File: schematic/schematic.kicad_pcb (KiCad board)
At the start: 2 copper layers, 99.1 x 99.1 mm, 0 parts

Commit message: d
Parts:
- added AE1: Antenna_Chip, RF_Antenna:Johanson_2450AT18x100, F.Cu at (220.8, 44.4)
- added BT1: Battery_Cell, Connector_PinHeader_2.54mm:PinHeader_1x02_P2.54mm_Vertical, F.Cu at (99.9, 69.8)
- added BT2: Battery_Cell, Connector_PinHeader_2.54mm:PinHeader_1x02_P2.54mm_Vertical, F.Cu at (100.1, 77.1)
- added BT3: Battery_Cell, Connector_PinHeader_2.54mm:PinHeader_1x02_P2.54mm_Vertical, F.Cu at (100.3, 84.6)
- added C1: 3.797pF, Capacitor_SMD:C_0805_2012Metric_Pad1.18x1.45mm_HandSolder, F.Cu at (230.8, 44.2)
- added C10: 100nF, Capacitor_SMD:C_0805_2012Metric_Pad1.18x1.45mm_HandSolder, F.Cu at (226.0, 44.2)
- added C11: 84nF, Capacitor_SMD:C_0805_2012Metric_Pad1.18x1.45mm_HandSolder, F.Cu at (198.0, 44.2)
- added C12: 1uF, Capacitor_SMD:C_0805_2012Metric_Pad1.18x1.45mm_HandSolder, F.Cu at (193.2, 50.2)
- added C13: 1uF, Capacitor_SMD:C_0805_2012Metric_Pad1.18x1.45mm_HandSolder, F.Cu at (193.2, 47.2)
- added C14: 100nF, Capacitor_SMD:C_0805_2012Metric_Pad1.18x1.45mm_HandSolder, F.Cu at (185.5, 44.0)
- added C15: 10uF, Capacitor_SMD:C_0805_2012Metric_Pad1.18x1.45mm_HandSolder, F.Cu at (111.4, 60.9)
- added C16: 100nF, Capacitor_SMD:C_0805_2012Metric_Pad1.18x1.45mm_HandSolder, F.Cu at (176.7, 61.3)
- added C19: 10uF, Capacitor_SMD:C_0805_2012Metric_Pad1.18x1.45mm_HandSolder, F.Cu at (176.7, 64.3)
- added C2: 4.64pF, Capacitor_SMD:C_0805_2012Metric_Pad1.18x1.45mm_HandSolder, F.Cu at (229.9, 47.2)
- added C20: 10uF, Capacitor_SMD:C_0805_2012Metric_Pad1.18x1.45mm_HandSolder, F.Cu at (186.9, 56.8)
- added C21: 100nF, Capacitor_SMD:C_0805_2012Metric_Pad1.18x1.45mm_HandSolder, F.Cu at (107.9, 61.0)
- added C22: 1uF, Capacitor_SMD:C_0805_2012Metric_Pad1.18x1.45mm_HandSolder, F.Cu at (181.1, 58.2)
- added C23: 1uF, Capacitor_SMD:C_0805_2012Metric_Pad1.18x1.45mm_HandSolder, F.Cu at (155.8, 80.0)
- added C3: 3.3nF, Capacitor_SMD:C_0805_2012Metric_Pad1.18x1.45mm_HandSolder, F.Cu at (219.7, 54.4)
- added C4: 10nF, Capacitor_SMD:C_0805_2012Metric_Pad1.18x1.45mm_HandSolder, F.Cu at (224.5, 50.6)
- added C5: 100nF, Capacitor_SMD:C_0805_2012Metric_Pad1.18x1.45mm_HandSolder, F.Cu at (225.1, 47.6)
- added C6: 10pF, Capacitor_SMD:C_0805_2012Metric_Pad1.18x1.45mm_HandSolder, F.Cu at (220.3, 47.6)
- added C7: 10pF, Capacitor_SMD:C_0805_2012Metric_Pad1.18x1.45mm_HandSolder, F.Cu at (219.7, 51.4)
- added C8: 100nF, Capacitor_SMD:C_0805_2012Metric_Pad1.18x1.45mm_HandSolder, F.Cu at (224.5, 53.6)
- added C9: 84nF, Capacitor_SMD:C_0805_2012Metric_Pad1.18x1.45mm_HandSolder, F.Cu at (174.4, 67.5)
- added D1: ZMM3V9, Diode_SMD:D_MiniMELF, F.Cu at (144.9, 96.4)
- added D2: ZMM3V9, Diode_SMD:D_MiniMELF, F.Cu at (138.6, 96.4)
- added D4: SS34, Diode_SMD:D_SMA_Handsoldering, B.Cu at (114.5, 62.3)
- added J1: Peltier Connection, Connector_PinHeader_2.54mm:PinHeader_1x02_P2.54mm_Vertical, F.Cu at (151.5, 88.7)
- added J2: USB_C_Receptacle_USB2.0, 1KicadLib:USB4125-GF-A, F.Cu at (103.4, 58.9)
- added J4: Serial, Connector_PinHeader_2.54mm:PinHeader_1x03_P2.54mm_Vertical, F.Cu at (139.9, 104.0)
- added L1: 1.807nH, Inductor_SMD:L_0805_2012Metric_Pad1.15x1.40mm_HandSolder, F.Cu at (235.6, 44.2)
- added L2: 33uH, Inductor_SMD:L_10.4x10.4_H4.8, F.Cu at (159.4, 48.7)
- added L3: 33uH, Inductor_SMD:L_10.4x10.4_H4.8, B.Cu at (119.1, 54.5)
- added L4: 33uH, Inductor_SMD:L_10.4x10.4_H4.8, F.Cu at (152.8, 66.1)
- added R1: 20k, Resistor_SMD:R_0805_2012Metric_Pad1.20x1.40mm_HandSolder, F.Cu at (229.3, 50.6)
- added R10: 7.5k, Resistor_SMD:R_0805_2012Metric_Pad1.20x1.40mm_HandSolder, F.Cu at (181.5, 61.2)
- added R11: 15k, Resistor_SMD:R_0805_2012Metric_Pad1.20x1.40mm_HandSolder, F.Cu at (137.1, 116.9)
- added R12: 28.7, Resistor_SMD:R_2512_6332Metric_Pad1.40x3.35mm_HandSolder, F.Cu at (106.0, 71.3)
- added R13: 33k, Resistor_SMD:R_0805_2012Metric_Pad1.20x1.40mm_HandSolder, F.Cu at (191.7, 56.8)
- added R14: 110k, Resistor_SMD:R_0805_2012Metric_Pad1.20x1.40mm_HandSolder, F.Cu at (136.5, 120.8)
- added R15: 28.7, Resistor_SMD:R_2512_6332Metric_Pad1.40x3.35mm_HandSolder, F.Cu at (106.0, 79.4)
- added R16: 28.7, Resistor_SMD:R_2512_6332Metric_Pad1.40x3.35mm_HandSolder, F.Cu at (106.1, 87.5)
- added R17: 200, Resistor_SMD:R_0805_2012Metric_Pad1.20x1.40mm_HandSolder, F.Cu at (121.4, 70.2)
- added R18: 200, Resistor_SMD:R_0805_2012Metric_Pad1.20x1.40mm_HandSolder, F.Cu at (121.1, 77.9)
- added R19: 200, Resistor_SMD:R_0805_2012Metric_Pad1.20x1.40mm_HandSolder, F.Cu at (121.3, 86.1)
- added R2: 39k, Resistor_SMD:R_0805_2012Metric_Pad1.20x1.40mm_HandSolder, F.Cu at (165.4, 78.4)
- added R20: 90k, Resistor_SMD:R_0805_2012Metric_Pad1.20x1.40mm_HandSolder, F.Cu at (213.0, 65.6)
- added R21: 90k, Resistor_SMD:R_0805_2012Metric_Pad1.20x1.40mm_HandSolder, F.Cu at (213.0, 68.5)
- added R22: 180k, Resistor_SMD:R_0805_2012Metric_Pad1.20x1.40mm_HandSolder, F.Cu at (122.7, 102.6)
- added R23: 36k, Resistor_SMD:R_0805_2012Metric_Pad1.20x1.40mm_HandSolder, F.Cu at (119.4, 103.8)
- added R24: 90k, Resistor_SMD:R_0805_2012Metric_Pad1.20x1.40mm_HandSolder, F.Cu at (222.5, 62.6)
- added R25: 4.3k, Resistor_SMD:R_0805_2012Metric_Pad1.20x1.40mm_HandSolder, F.Cu at (123.0, 105.8)
- added R26: 180k, Resistor_SMD:R_0805_2012Metric_Pad1.20x1.40mm_HandSolder, F.Cu at (124.4, 99.6)
- added R27: 68k, Resistor_SMD:R_0805_2012Metric_Pad1.20x1.40mm_HandSolder, F.Cu at (123.4, 95.0)
- added R28: 510k, Resistor_SMD:R_0805_2012Metric_Pad1.20x1.40mm_HandSolder, F.Cu at (117.9, 95.6)
- added R29: 620k, Resistor_SMD:R_0805_2012Metric_Pad1.20x1.40mm_HandSolder, F.Cu at (118.4, 98.7)
- added R3: 39k, Resistor_SMD:R_0805_2012Metric_Pad1.20x1.40mm_HandSolder, F.Cu at (202.8, 44.2)
- added R30: 200k, Resistor_SMD:R_0805_2012Metric_Pad1.20x1.40mm_HandSolder, B.Cu at (105.2, 100.9)
- added R31: 51k, Resistor_SMD:R_0805_2012Metric_Pad1.20x1.40mm_HandSolder, B.Cu at (109.1, 100.9)
- added R33: 500, Resistor_SMD:R_0805_2012Metric_Pad1.20x1.40mm_HandSolder, F.Cu at (102.8, 97.7)
- added R34: 12.5k, Resistor_SMD:R_0805_2012Metric_Pad1.20x1.40mm_HandSolder, B.Cu at (106.5, 94.7)
- added R39: 150k, Resistor_SMD:R_0805_2012Metric_Pad1.20x1.40mm_HandSolder, F.Cu at (224.5, 56.6)
- added R4: .1, Resistor_SMD:R_1206_3216Metric_Pad1.30x1.75mm_HandSolder, F.Cu at (100.7, 91.9)
- added R40: 100k, Resistor_SMD:R_0805_2012Metric_Pad1.20x1.40mm_HandSolder, F.Cu at (234.7, 47.2)
- added R5: 1k, Resistor_SMD:R_0805_2012Metric_Pad1.20x1.40mm_HandSolder, F.Cu at (104.2, 93.6)
- added R6: 1k, Resistor_SMD:R_0805_2012Metric_Pad1.20x1.40mm_HandSolder, B.Cu at (107.5, 97.7)
- added R7: 12.5k, Resistor_SMD:R_0805_2012Metric_Pad1.20x1.40mm_HandSolder, B.Cu at (103.3, 94.6)
- added R8: 5.1k, Resistor_SMD:R_0805_2012Metric_Pad1.20x1.40mm_HandSolder, B.Cu at (104.3, 59.5)
- added R9: 5.1k, Resistor_SMD:R_0805_2012Metric_Pad1.20x1.40mm_HandSolder, B.Cu at (102.2, 57.4)
- added SW1: Power Switch, Connector_PinHeader_2.54mm:PinHeader_1x02_P2.54mm_Vertical, F.Cu at (114.1, 66.1)
- added TH1: SDNT2012X103F3950FTF, Resistor_SMD:R_0805_2012Metric_Pad1.20x1.40mm_HandSolder, F.Cu at (213.0, 62.6)
- added TH2: SDNT2012X103F3950FTF, Resistor_SMD:R_0805_2012Metric_Pad1.20x1.40mm_HandSolder, F.Cu at (217.8, 62.6)
- added TH3: SDNT2012X103F3950FTF, Resistor_SMD:R_0805_2012Metric_Pad1.20x1.40mm_HandSolder, F.Cu at (217.8, 65.6)
- added U1: ESP32-D-WD-V3, Package_DFN_QFN:QFN-48-1EP_5x5mm_P0.35mm_EP3.7x3.7mm, F.Cu at (222.0, 97.6)
- added U10: BSD316, Package_TO_SOT_SMD:SOT-363_SC-70-6_Handsoldering, B.Cu at (105.9, 82.9)
- added U11: BSD316, Package_TO_SOT_SMD:SOT-363_SC-70-6_Handsoldering, B.Cu at (105.9, 90.3)
- added U12: PC817, Package_DIP:DIP-4_W7.62mm, B.Cu at (118.3, 70.2)
- added U13: PC817, Package_DIP:DIP-4_W7.62mm, B.Cu at (118.1, 77.9)
- added U14: PC817, Package_DIP:DIP-4_W7.62mm, B.Cu at (118.2, 86.1)
- added U15: AS431, Package_TO_SOT_SMD:SOT-23-5_HandSoldering, F.Cu at (99.3, 97.7)
- added U17: XL6009, Package_TO_SOT_SMD:TO-263-5_TabPin3, F.Cu at (118.3, 53.0)
- added U18: slg55021, 1KicadLib:TDFN_8_2x2mm_EP_0.9x1.65mm, F.Cu at (150.9, 105.4)
- added U19: AOZ6662DI, 1KicadLib:DFN_8_3x3mm_EP_1.25x2.7mm, F.Cu at (184.1, 48.8)
- added U2: NL17SZ14, Package_TO_SOT_SMD:SOT-553, F.Cu at (155.5, 91.2)
- added U20: AOZ6662DI, 1KicadLib:DFN_8_3x3mm_EP_1.25x2.7mm, F.Cu at (169.4, 69.1)
- added U3: BUK9K52-60E, 1KicadLib:LFPAK56D, F.Cu at (148.4, 92.1)
- added U4: BUK9K52-60E, 1KicadLib:LFPAK56D, F.Cu at (141.5, 92.1)
- added U5: LM324, Package_SO:SOIC-14_3.9x8.7mm_P1.27mm, F.Cu at (109.1, 97.2)
- added U6: slg55021, 1KicadLib:TDFN_8_2x2mm_EP_0.9x1.65mm, F.Cu at (150.9, 101.1)
- added U7: NL17SZ14, Package_TO_SOT_SMD:SOT-553, F.Cu at (155.5, 88.0)
- added U8: NL17SZ14, Package_TO_SOT_SMD:SOT-553, F.Cu at (150.9, 95.2)
- added U9: BSD316, Package_TO_SOT_SMD:SOT-363_SC-70-6_Handsoldering, B.Cu at (105.9, 74.7)
- added Y1: Crystal_GND24, Crystal:Crystal_SMD_SeikoEpson_FA238-4Pin_3.2x2.5mm_HandSoldering, F.Cu at (214.0, 52.8)
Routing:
- net Net-(R30-Pad2): track 0.00 -> 1.27 mm, vias 0 -> 1
- net Net-(R5-Pad1): vias 0 -> 1
- net Net-(R34-Pad2): vias 0 -> 1
- net Net-(R34-Pad1): vias 0 -> 1

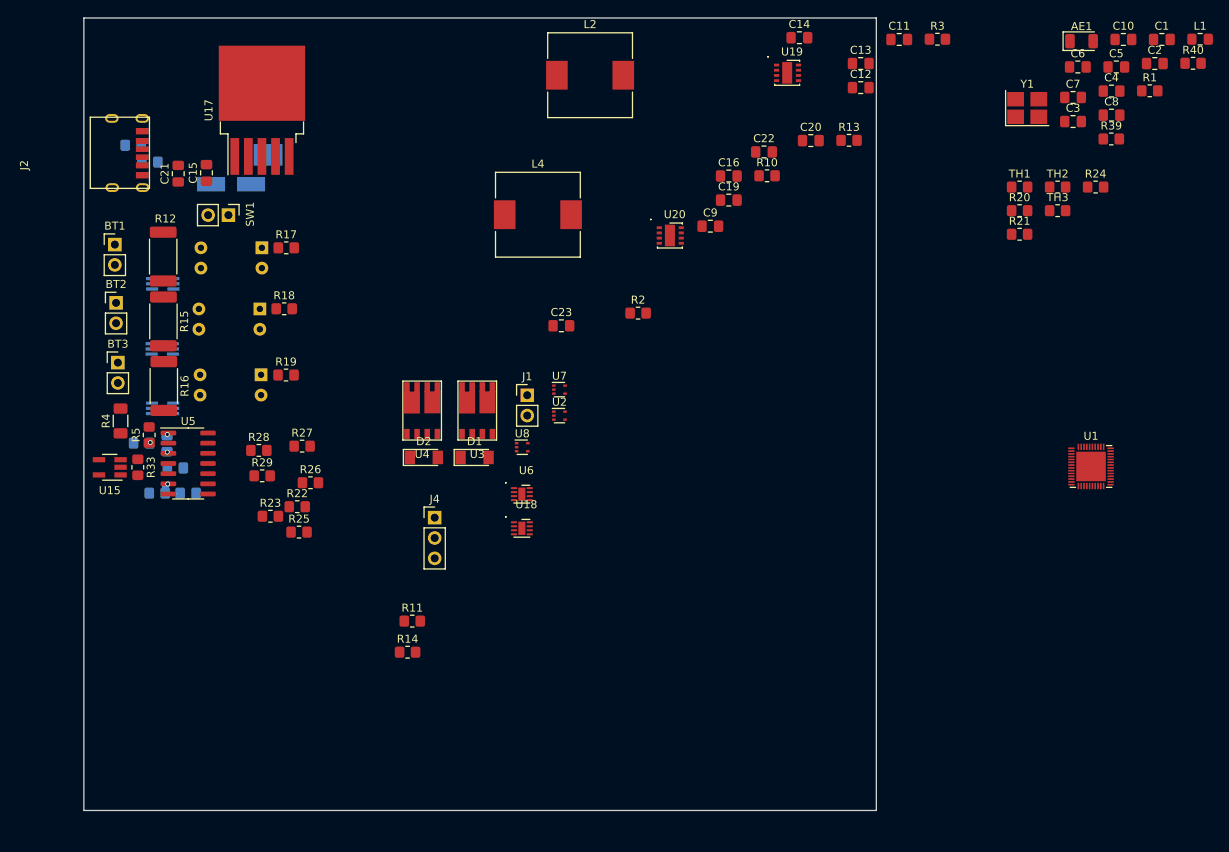
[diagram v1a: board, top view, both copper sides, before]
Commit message: beta boards routed
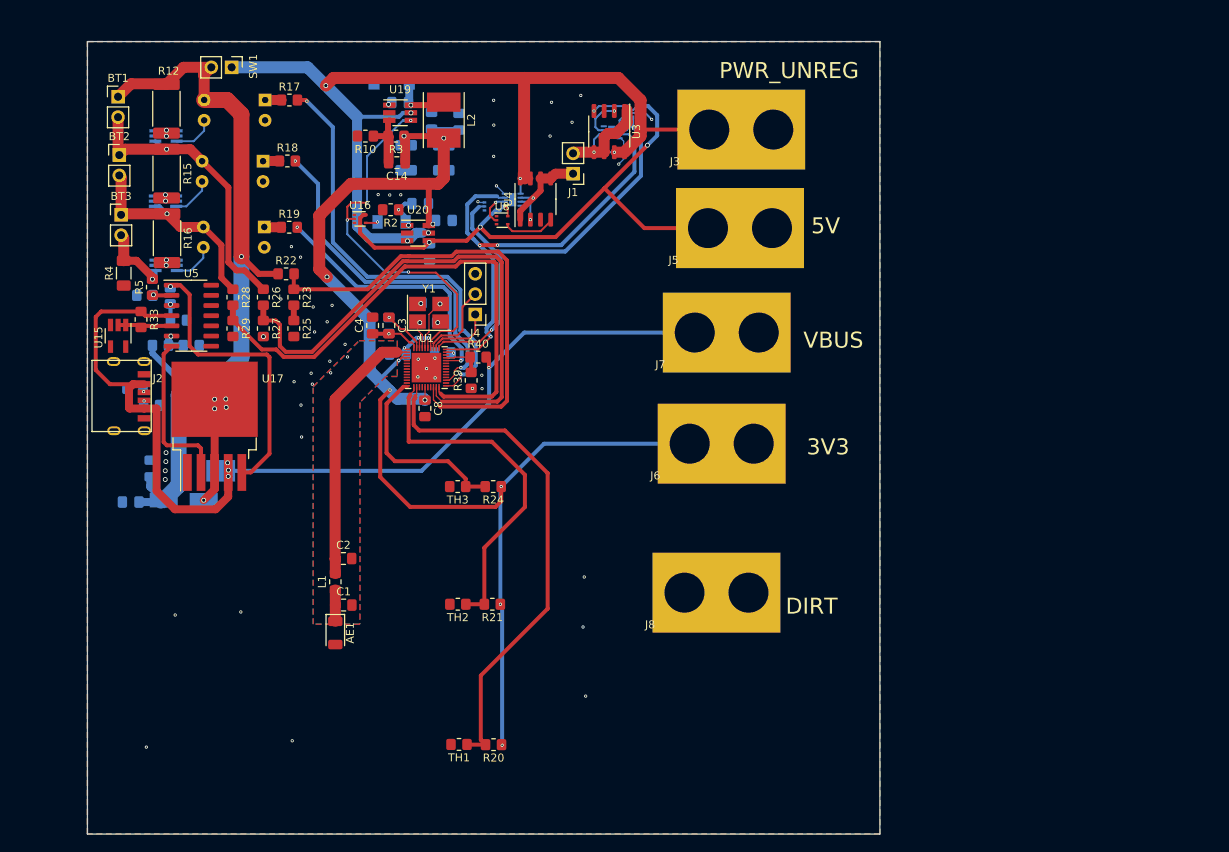
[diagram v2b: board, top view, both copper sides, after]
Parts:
- removed C20: 10uF, Capacitor_SMD:C_0805_2012Metric_Pad1.18x1.45mm_HandSolder
- removed C23: 1uF, Capacitor_SMD:C_0805_2012Metric_Pad1.18x1.45mm_HandSolder
- removed D1, D2: ZMM3V9, Diode_SMD:D_MiniMELF
- removed L4: 33uH, Inductor_SMD:L_10.4x10.4_H4.8
- removed R11: 15k, Resistor_SMD:R_0805_2012Metric_Pad1.20x1.40mm_HandSolder
- removed R13: 33k, Resistor_SMD:R_0805_2012Metric_Pad1.20x1.40mm_HandSolder
- removed R14: 110k, Resistor_SMD:R_0805_2012Metric_Pad1.20x1.40mm_HandSolder
- added C17: 100nF, Capacitor_SMD:C_0805_2012Metric_Pad1.18x1.45mm_HandSolder, B.Cu at (141.1, 66.8)
- added D3: LL4148, Diode_SMD:D_MiniMELF, B.Cu at (134.5, 67.0)
- added D5: PMEG40T20EPX, Diode_SMD:D_SOD-128, B.Cu at (134.5, 49.4)
- added J3: Conn_01x01_Male, 1KicadLib:GatorTestpoint, F.Cu at (169.8, 54.1)
- added J5: Conn_01x01_Male, 1KicadLib:GatorTestpoint, F.Cu at (169.6, 66.5)
- added J6: Conn_01x01_Male, 1KicadLib:GatorTestpoint, F.Cu at (167.3, 93.4)
- added J7: Conn_01x01_Male, 1KicadLib:GatorTestpoint, F.Cu at (167.9, 79.5)
- added J8: Conn_01x01_Male, 1KicadLib:GatorTestpoint, F.Cu at (166.7, 112.0)
- added U16: NL17SZ14, Package_TO_SOT_SMD:SOT-553, F.Cu at (130.6, 66.6)
- C10, C15, C16, C19, C21, C22, C5, C6, C7, R1, U18, U2, U6, U7: moved to B.Cu
- C11: value 84nF -> 2.2uF; moved to B.Cu
- C12, C13: value 1uF -> 100uF; footprint Capacitor_SMD:C_0805_2012Metric_Pad1.18x1.45mm_HandSolder -> Capacitor_SMD:C_1210_3225Metric_Pad1.33x2.70mm_HandSolder; moved to B.Cu
- C14: value 100nF -> 130pF
- C9: value 84nF -> 1uF; moved to B.Cu
- L2: value 33uH -> 3.3uH NRS5024T3R3NMGJ; footprint Inductor_SMD:L_10.4x10.4_H4.8 -> Inductor_SMD:L_Taiyo-Yuden_NR-50xx_HandSoldering
- R10: value 7.5k -> 27k
- R2: value 39k -> 300k
- R3: value 39k -> 62k
- U19: value AOZ6662DI -> XC9247B75CMR-G; footprint 1KicadLib:DFN_8_3x3mm_EP_1.25x2.7mm -> Package_TO_SOT_SMD:SOT-23-6_Handsoldering
- U20: value AOZ6662DI -> MIC5211; footprint 1KicadLib:DFN_8_3x3mm_EP_1.25x2.7mm -> Package_TO_SOT_SMD:SOT-23-6_Handsoldering
- U3, U4: value BUK9K52-60E -> DMT3020LSDQ; footprint 1KicadLib:LFPAK56D -> Package_SO:SO-8_3.9x4.9mm_P1.27mm
- moved L1 127.6 mm to (127.5, 112.0), turned to 90 degrees
- moved C1 124.3 mm to (128.5, 114.9)
- moved AE1 119.0 mm to (127.5, 118.4), turned to -90 degrees
- moved C2 118.8 mm to (128.5, 109.1)
- moved R1 99.5 mm to (134.2, 79.9), turned to -90 degrees
- moved TH1 98.8 mm to (143.0, 132.3), turned to 180 degrees
- moved C4 96.9 mm to (132.2, 79.9), turned to 90 degrees
- moved C5 96.7 mm to (135.3, 83.5), turned to 180 degrees
- moved R40 96.6 mm to (145.4, 83.9)
- moved R20 93.7 mm to (147.3, 132.3), turned to 180 degrees
- moved C10 93.7 mm to (140.9, 83.4), turned to 180 degrees
- moved C8 93.3 mm to (138.7, 90.3), turned to -90 degrees
- moved TH2 91.3 mm to (142.8, 114.8), turned to 180 degrees
- moved C3 89.2 mm to (134.2, 79.9), turned to -90 degrees
- moved C6 87.2 mm to (139.1, 79.5)
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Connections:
- C10 pad 1: +3V3 -> Net-(C10-Pad1)
- C11 pad 2: GND -> Net-(C11-Pad2)
- C12 pad 1: Net-(C12-Pad1) -> +3V3
- C13 pad 1: Net-(C13-Pad1) -> +3V3
- C14 pad 1: Net-(C14-Pad1) -> +3V3
- C16 pad 1: Net-(C16-Pad1) -> +5V
- C16 pad 2: Net-(C16-Pad2) -> GND
- L2 pad 1: Net-(C14-Pad2) -> Net-(C11-Pad2)
- R10 pad 1: Net-(R10-Pad1) -> Net-(C14-Pad2)
- R2 pad 2: Net-(R2-Pad2) -> GND
- R3 pad 1: Net-(C11-Pad1) -> +3V3
- R3 pad 2: Net-(R3-Pad2) -> Net-(C14-Pad2)
- SW1 pad 1: VCC_UNREGULATED -> PWR_UNREG
- U1 pad 11: DRIVER -> unconnected-(U1-Pad11)
- U1 pad 12: TEMP_SENSE_1 -> unconnected-(U1-Pad12)
- U1 pad 13: TEMP_SENSE_2 -> unconnected-(U1-Pad13)
- U1 pad 15: unconnected-(U1-Pad15) -> TEMP_SENSE_2
- U1 pad 16: MOS_VDRIVE_PWM -> TEMP_SENSE_1
- U1 pad 37: +3V3 -> Net-(C10-Pad1)
- U1 pad 38: unconnected-(U1-Pad38) -> DRIVER_EN
- U1 pad 39: unconnected-(U1-Pad39) -> ~DRIVER_DIR
- U1 pad 42: unconnected-(U1-Pad42) -> TURBO_EN
- U18 pad 3: ~DRIVER_EN -> DRIVER_EN
- U18 pad 5: VCC_UNREGULATED -> PWR_UNREG
- U18 pad 7: Net-(D2-Pad1) -> Net-(U18-Pad7)
- U19 pad 1: GND -> Net-(C11-Pad1)
- U19 pad 2: Net-(C14-Pad2) -> GND
- U19 pad 3: VCC_UNREGULATED -> Net-(C14-Pad2)
- U19 pad 4: Net-(R2-Pad2) -> TURBO_EN
- U19 pad 5: Net-(C12-Pad1) -> PWR_UNREG
- U19 pad 6: Net-(R10-Pad1) -> Net-(C11-Pad2)
- U20 pad 1: GND -> Net-(C9-Pad1)
- U20 pad 2: Net-(C16-Pad2) -> GND
- U20 pad 3: VCC_UNREGULATED -> PWR_UNREG
- U20 pad 4: Net-(R3-Pad2) -> +5V
- U20 pad 5: Net-(C13-Pad1) -> PWR_UNREG
- U20 pad 6: Net-(R11-Pad1) -> +3V3
- U3 pad 2: Net-(D1-Pad2) -> Net-(U3-Pad2)
- U3 pad 7: VCC_UNREGULATED -> PWR_UNREG
- U3 pad 8: VCC_UNREGULATED -> PWR_UNREG
- U4 pad 2: Net-(D2-Pad2) -> Net-(U18-Pad7)
- U4 pad 7: VCC_UNREGULATED -> PWR_UNREG
- U4 pad 8: VCC_UNREGULATED -> PWR_UNREG
- U6 pad 3: ~DRIVER_EN -> DRIVER_EN
- U6 pad 5: VCC_UNREGULATED -> PWR_UNREG
- U6 pad 7: Net-(D1-Pad1) -> Net-(U3-Pad2)
- U8 pad 2: Net-(U4-Pad4) -> Net-(U18-Pad2)
- U8 pad 4: Net-(U18-Pad2) -> Net-(U4-Pad4)
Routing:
- net +3V3: track 0.00 -> 179.0 mm, vias 0 -> 13
- net PWR_UNREG: track 0.00 -> 125.1 mm, vias 0 -> 6
- net VBUS: track 0.00 -> 124.4 mm, vias 0 -> 4
- net +BATT: track 0.00 -> 97.3 mm, vias 0 -> 1
- net +5V: track 0.00 -> 77.4 mm, vias 0 -> 4
- net CELL_MEAS_2: track 0.00 -> 66.7 mm
- net CELL_MEAS_1: track 0.00 -> 66.1 mm
- net TEMP_SENSE_1: track 0.00 -> 64.1 mm
- net CELL_MEAS_3: track 0.00 -> 59.8 mm
- net DRIVER_EN: track 0.00 -> 59.2 mm, vias 0 -> 3
- net ~DRIVER_DIR: track 0.00 -> 57.8 mm, vias 0 -> 1
- net CELL_DSCHG_3: track 0.00 -> 54.2 mm, vias 0 -> 2
- net TURBO_EN: track 0.00 -> 46.1 mm, vias 0 -> 4
- net CELL_DSCHG_2: track 0.00 -> 44.0 mm, vias 0 -> 2
- net TEMP_SENSE_2: track 0.00 -> 43.9 mm
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- added copper zone on B.Cu, net GND
- added copper zone on F.Cu, net GND
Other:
- board text added: "3V3"
- board text added: "5V"
- board text added: "DIRT"
- board text added: "PWR_UNREG"
- board text added: "VBUS"

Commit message: prelim ble working
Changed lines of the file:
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@@
   (segment (start 135.9662 53.3654) (end 136.9568 53.3654) (width 0.5) (layer "B.Cu") (net 77))
   (segment (start 114.5476 47.667) (end 124.0448 47.667) (width 1.5) (layer "B.Cu") (net 77))
-  (segment (start 138.3792 68.3514) (end 137.5918 68.3514) (width 1.25) (layer "B.Cu") (net 77))
+  (segment (start 138.3792 68.3514) (end 137.5918 68.3514) (width 1) (layer "B.Cu") (net 77))
   (segment (start 124.0448 47.667) (end 130.2258 53.848) (width 1.5) (layer "B.Cu") (net 77))
   (segment (start 130.2258 67.5132) (end 130.2258 53.848) (width 1.25) (layer "B.Cu") (net 77))

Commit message: e
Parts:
- removed C16, C17: 100nF, Capacitor_SMD:C_0805_2012Metric_Pad1.18x1.45mm_HandSolder
- removed C19: 10uF, Capacitor_SMD:C_0805_2012Metric_Pad1.18x1.45mm_HandSolder
- removed C22: 1uF, Capacitor_SMD:C_0805_2012Metric_Pad1.18x1.45mm_HandSolder
- removed D3: LL4148, Diode_SMD:D_MiniMELF
- removed D5: PMEG40T20EPX, Diode_SMD:D_SOD-128
- removed R10: 27k, Resistor_SMD:R_0805_2012Metric_Pad1.20x1.40mm_HandSolder
- removed U20: MIC5211, Package_TO_SOT_SMD:SOT-23-6_Handsoldering
- C11: value 2.2uF -> 100nF; moved to F.Cu
- C12: value 100uF -> 10uF; footprint Capacitor_SMD:C_1210_3225Metric_Pad1.33x2.70mm_HandSolder -> Capacitor_SMD:C_0805_2012Metric_Pad1.18x1.45mm_HandSolder; moved to F.Cu
- C13: value 100uF -> 22uF; footprint Capacitor_SMD:C_1210_3225Metric_Pad1.33x2.70mm_HandSolder -> Capacitor_SMD:C_0805_2012Metric_Pad1.18x1.45mm_HandSolder; moved to F.Cu
- C14: value 130pF -> 22uF
- C9: value 1uF -> 10uF; moved to F.Cu
- R2: value 300k -> 0
- R3: value 62k -> 0
- U16: value NL17SZ14 -> AP63203WU; footprint Package_TO_SOT_SMD:SOT-553 -> Package_TO_SOT_SMD:TSOT-23-6
- U19: value XC9247B75CMR-G -> HT75xx-1-SOT89; footprint Package_TO_SOT_SMD:SOT-23-6_Handsoldering -> Package_TO_SOT_SMD:SOT-89-3
- moved L2 43.9 mm to (155.9, 95.6), turned to 0 degrees
- moved C14 43.4 mm to (161.9, 93.8), turned to 0 degrees
- moved C11 41.4 mm to (152.1, 90.1), turned to -90 degrees
- moved C13 37.3 mm to (161.2, 90.4), turned to 0 degrees
- moved R3 34.9 mm to (154.4, 85.4)
- moved U16 34.7 mm to (156.7, 89.5), turned to 180 degrees
- moved R24 31.8 mm to (147.1, 131.9)
- moved TH3 31.8 mm to (142.6, 131.9)
- moved TH1 31.8 mm to (142.6, 100.6)
- moved R20 31.8 mm to (146.9, 100.6)
- moved R2 10.4 mm to (139.7, 56.5), turned to 0 degrees
- moved C9 6.49 mm to (133.9, 59.8), turned to -90 degrees
- moved U19 1.99 mm to (134.7, 55.1), turned to 90 degrees
- moved C12 1.45 mm to (137.3, 60.1)
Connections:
- net VBUS renamed USB_PWR
- C12 pad 1: +3V3 -> +5V
- C14 pad 2: Net-(C14-Pad2) -> GND
- C5 pad 1: +3V3 -> /MCU/3V3_MCU
- C8 pad 1: +3V3 -> /MCU/3V3_MCU
- C9 pad 1: Net-(C9-Pad1) -> PWR_UNREG
- L2 pad 1: Net-(C11-Pad2) -> Net-(C11-Pad1)
- R2 pad 1: Net-(C9-Pad1) -> +5V
- R2 pad 2: GND -> /Peltier Driver/5V_PD
- R3 pad 2: Net-(C14-Pad2) -> /MCU/3V3_MCU
- U1 pad 1: +3V3 -> /MCU/3V3_MCU
- U1 pad 19: +3V3 -> /MCU/3V3_MCU
- U1 pad 3: +3V3 -> /MCU/3V3_MCU
- U1 pad 4: +3V3 -> /MCU/3V3_MCU
- U1 pad 42: TURBO_EN -> unconnected-(U1-Pad42)
- U1 pad 43: +3V3 -> /MCU/3V3_MCU
- U1 pad 46: +3V3 -> /MCU/3V3_MCU
- U16 pad 1: (no net) -> +3V3
- U16 pad 2: TURBO_EN -> PWR_UNREG
- U16 pad 3: GND -> PWR_UNREG
- U16 pad 4: Net-(D3-Pad2) -> GND
- U16 pad 5: +5V -> Net-(C11-Pad1)
- U18 pad 1: +5V -> /Peltier Driver/5V_PD
- U19 pad 1: Net-(C11-Pad1) -> GND
- U19 pad 2: GND -> PWR_UNREG
- U19 pad 3: Net-(C14-Pad2) -> +5V
- U2 pad 5: +5V -> /Peltier Driver/5V_PD
- U6 pad 1: +5V -> /Peltier Driver/5V_PD
- U7 pad 5: +5V -> /Peltier Driver/5V_PD
- U8 pad 5: +5V -> /Peltier Driver/5V_PD
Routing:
- net +3V3: track 179.0 -> 0.58 mm, vias 13 -> 0
- net +5V: track 77.4 -> 0.00 mm, vias 4 -> 0
- net PWR_UNREG: track 125.1 -> 61.0 mm, vias 6 -> 2
- net /Peltier Driver/5V_PD: track 0.00 -> 57.8 mm, vias 0 -> 3
- net TURBO_EN: track 46.1 -> 0.00 mm, vias 4 -> 0
- net TEMP_SENSE_1: track 64.1 -> 18.8 mm
- net TEMP_SENSE_3: track 24.2 -> 51.2 mm
- net /MCU/3V3_MCU: track 0.00 -> 13.2 mm, vias 0 -> 4
- net TEMP_SENSE_2: track 43.9 -> 32.7 mm
- net Net-(C14-Pad2): track 7.21 -> 0.00 mm
- net Net-(C11-Pad2): track 6.98 -> 0.00 mm, vias 1 -> 0
- net Net-(C9-Pad1): track 3.85 -> 0.00 mm, vias 2 -> 0
- net Net-(U2-Pad4): track 4.63 -> 6.33 mm
- net Net-(D3-Pad2): track 1.54 -> 0.00 mm, vias 1 -> 0
- net GND: track 9.64 -> 9.62 mm, vias 52 -> 49
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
